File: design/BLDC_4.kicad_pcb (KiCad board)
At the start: 4 copper layers, 141 x 61 mm, 233 parts, among them K1 SERVO, P1 CANBUS, P10 MOTOR3, P11 MOTOR2, P12 MOTOR1, P13 SWD, P14 IN+, P15 PWR_COMM_2, P2 HALL/Encoder, P3 HALL/Encoder, P4 PWR_COMM_1, P5 IN+, P6 IN-, P7 MOTOR3, P8 MOTOR2, P9 MOTOR1, Q1 FDBL0630N150, Q10 FDBL0630N150, Q11 FDBL0630N150, Q12 FDBL0630N150, Q2 FDBL0630N150, Q3 FDBL0630N150, Q4 FDBL0630N150, Q5 FDBL0630N150, Q6 FDBL0630N150, Q7 FDBL0630N150, Q8 FDBL0630N150, Q9 FDBL0630N150, U1 SN65HVD232, U2 DRV8302, U3 NCP1117ST33T3G, U4 STM32F40X_LQFP144, U5 DRV8302, U6 NCP1117ST33T3G, X1 MINI-USB-SHIELD-32005-201, X2 8MHz 10ppm

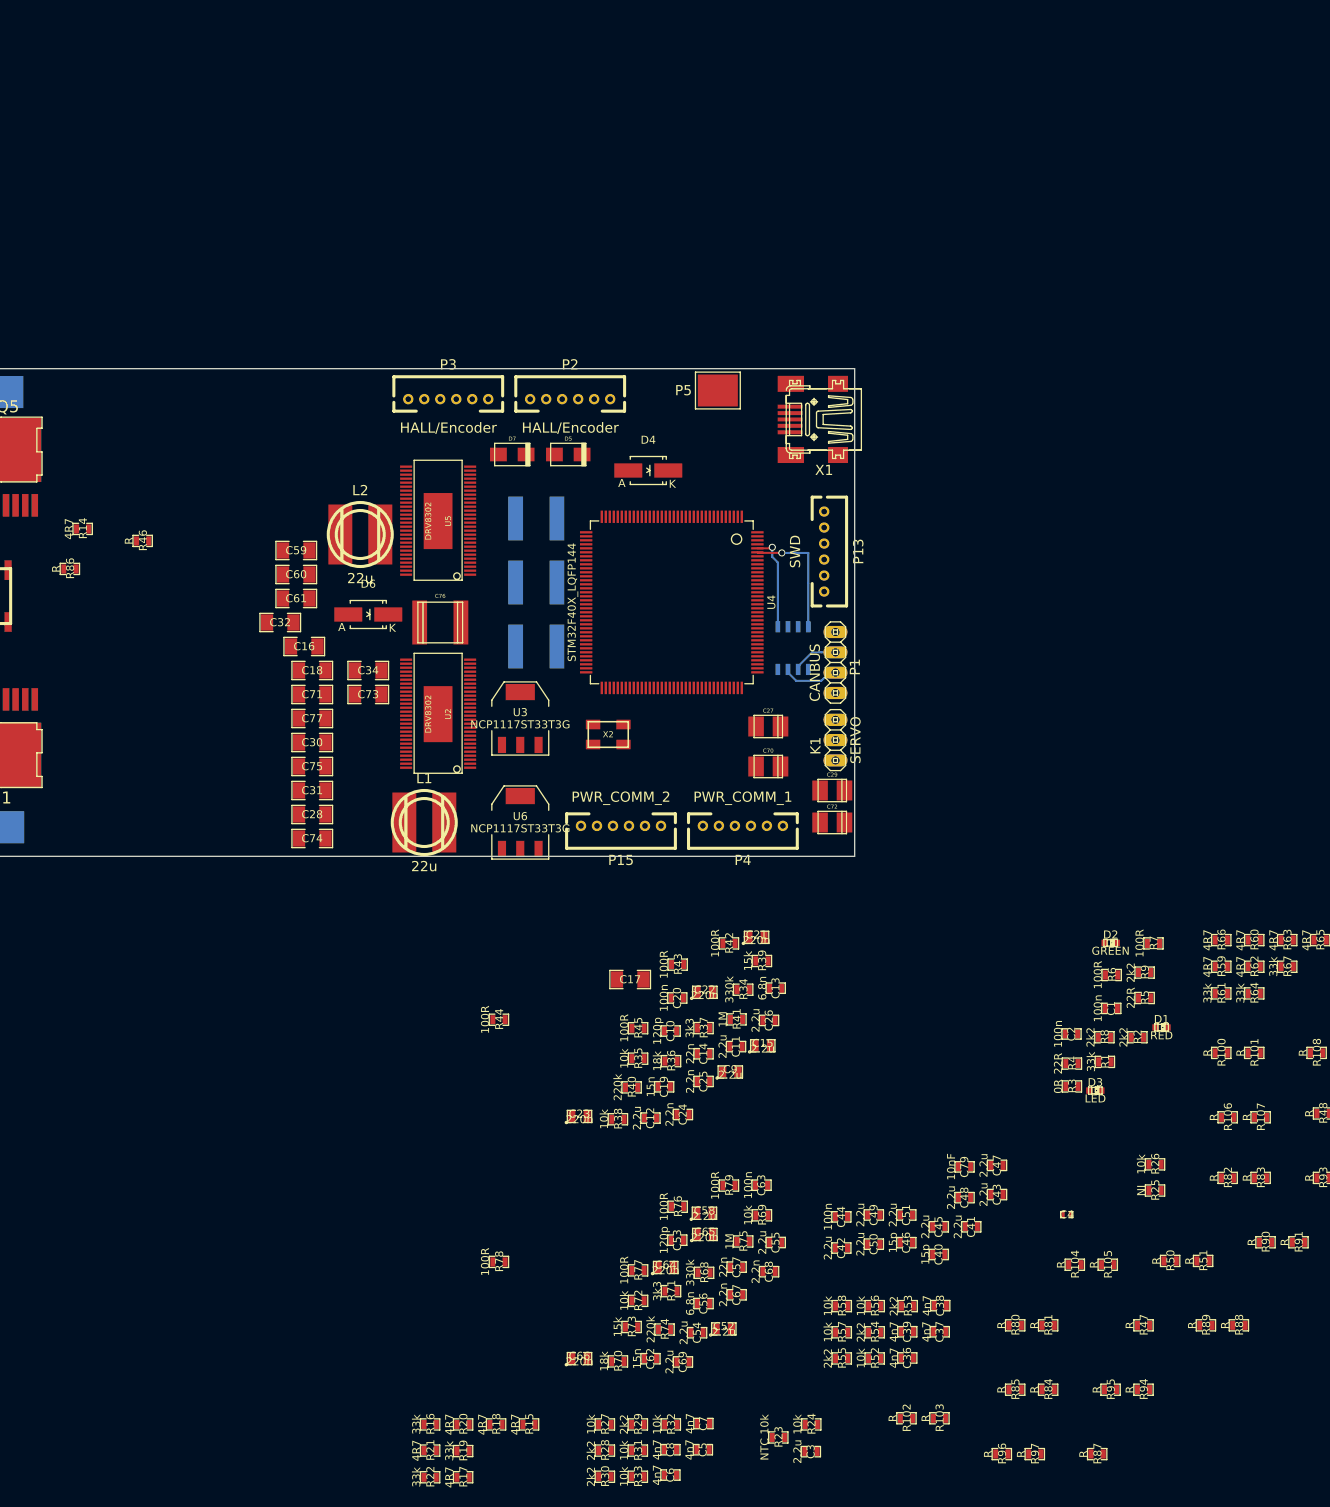
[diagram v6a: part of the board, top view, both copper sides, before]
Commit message: New desing starting placment of components
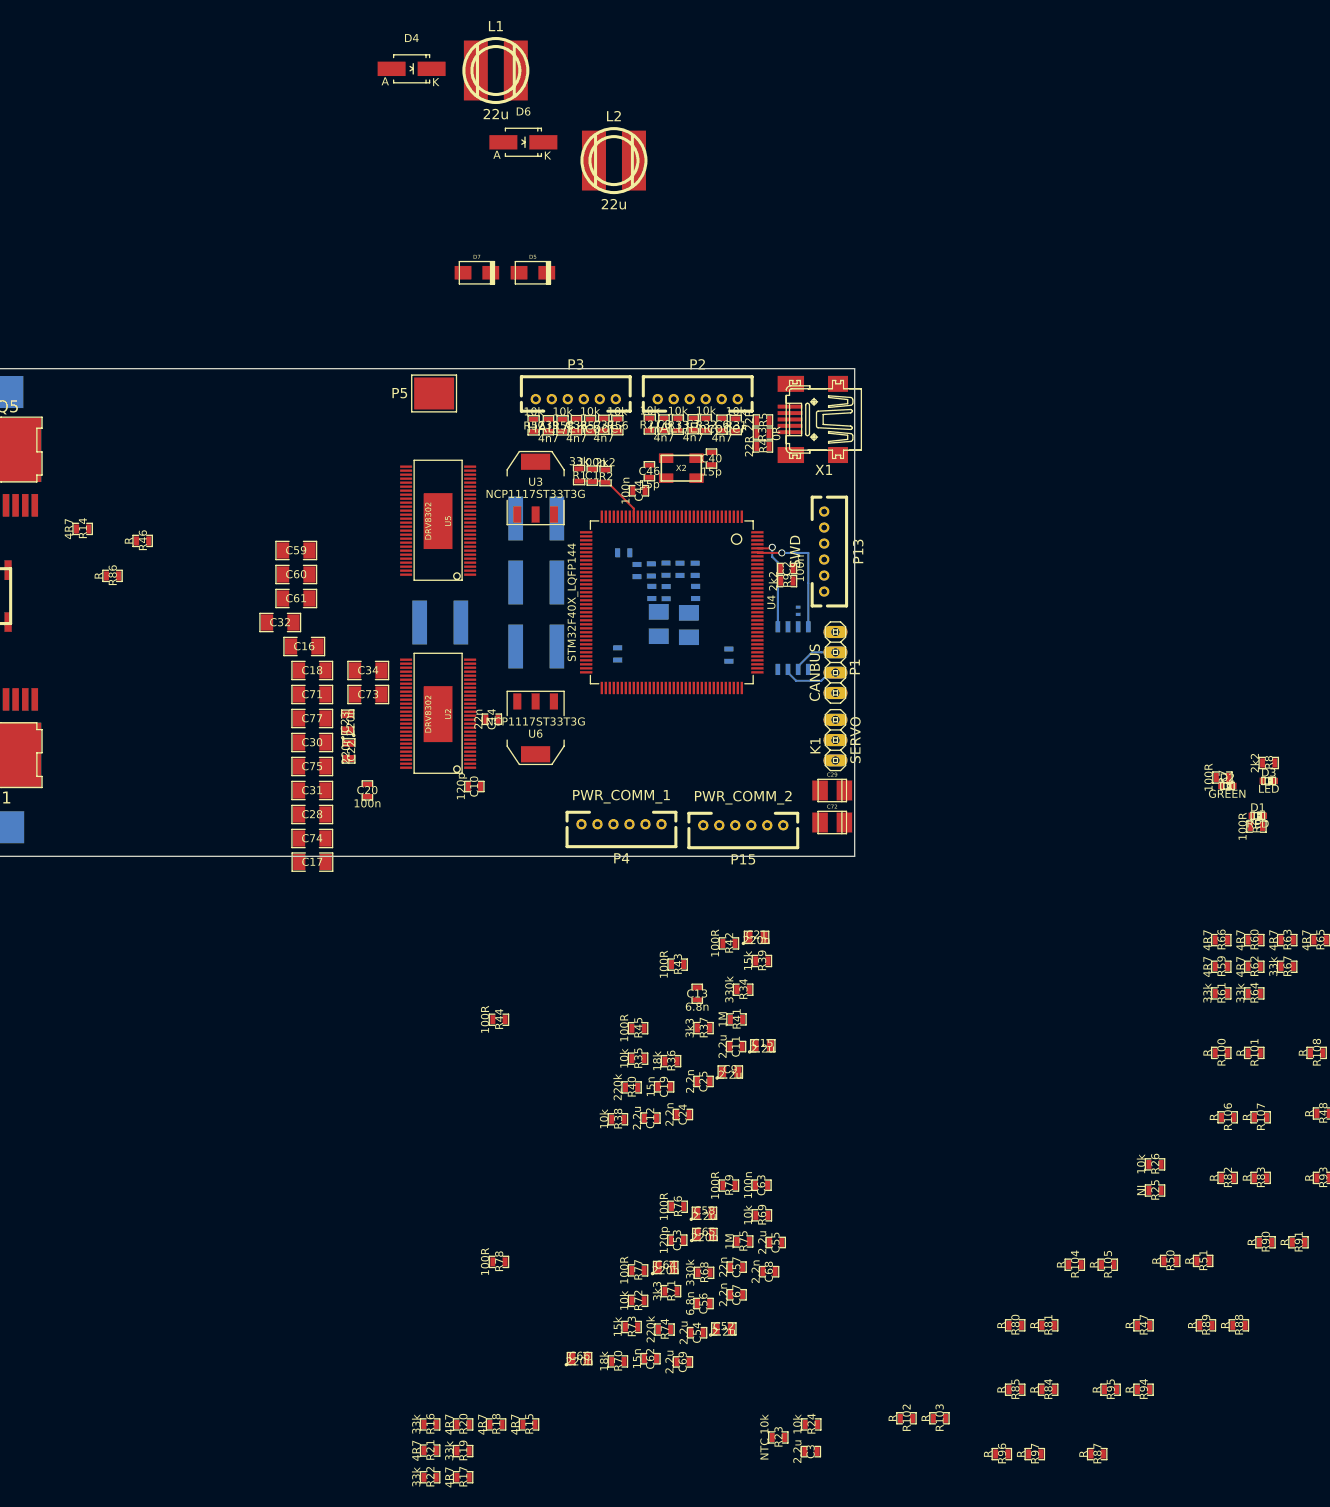
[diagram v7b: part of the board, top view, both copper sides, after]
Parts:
- C26, C27, C36, C4, C41, C42, C43, C45, C47, C48, C49, C5, C50, C51, C70, C76, C79, R28, R29, R30, R53, R54, R55: moved to B.Cu
- moved R30 131.8 mm to (155.7, 135.2), turned to 90 degrees
- moved R33 131.6 mm to (155.7, 135.3), turned to 270 degrees
- moved C6 131.5 mm to (161.2, 135.3), turned to 90 degrees
- moved R28 129.2 mm to (162.9, 135.3), turned to 270 degrees
- moved R31 128.8 mm to (162.9, 135.3), turned to 270 degrees
- moved C5 128.3 mm to (152.2, 135.2), turned to 90 degrees
- moved C8 128.2 mm to (154.0, 135.2), turned to 90 degrees
- moved C36 125.6 mm to (137.7, 135.4), turned to 90 degrees
- moved R29 125.3 mm to (159.2, 135.3), turned to 270 degrees
- moved R27 125.1 mm to (152.2, 135.2), turned to 270 degrees
- moved R32 125.1 mm to (159.2, 135.2), turned to 270 degrees
- moved C7 124.9 mm to (157.6, 135.2), turned to 90 degrees
- moved R52 124.2 mm to (137.7, 135.3), turned to 270 degrees
- moved C39 121.9 mm to (139.5, 135.3), turned to 90 degrees
- moved R55 121.8 mm to (141.3, 135.3), turned to 270 degrees
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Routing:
- net /MCU/AN_IN: track 0.00 -> 9.29 mm

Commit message: More layouting
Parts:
- C11, C12, C17, C18, C25, C28, C31, C64, L1, L2, R34, R35, R36, R37, R41, R44, R45, R6, R7, R8, U3: moved to B.Cu
- C76, C78: moved to F.Cu
- moved C64 206.1 mm to (183.8, 36.7)
- moved C69 200.8 mm to (202.9, 57.1), turned to 90 degrees
- moved C63 193.3 mm to (183.8, 37.8), turned to 270 degrees
- moved C12 168.4 mm to (201.1, 60.7), turned to 90 degrees
- moved C24 164.2 mm to (183.7, 59.6), turned to 270 degrees
- moved R38 162.1 mm to (199.6, 68.3)
- moved C72 160.3 mm to (174.6, 24.7)
- moved C25 159.7 mm to (183.8, 59.6), turned to 270 degrees
- moved C11 159.1 mm to (199.9, 58.3), turned to 270 degrees
- moved R44 158.5 mm to (181.5, 58.6)
- moved C15 158.3 mm to (200.5, 58.3), turned to 270 degrees
- moved R35 156.5 mm to (200.4, 66.1)
- moved C9 155.2 mm to (199.1, 65.4), turned to 90 degrees
- moved R45 153.4 mm to (181.3, 60.4)
- moved C17 153.2 mm to (184.6, 56.1)
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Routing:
- net Net-(K1-Pad1): track 0.00 -> 25.1 mm
- net /MCU/SERVO: track 0.00 -> 4.53 mm
